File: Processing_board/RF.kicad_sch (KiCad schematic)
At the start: 13 parts, among them J10 CONMHF1-SMD-G-T, U8 BGS13SN8E6327XTSA1

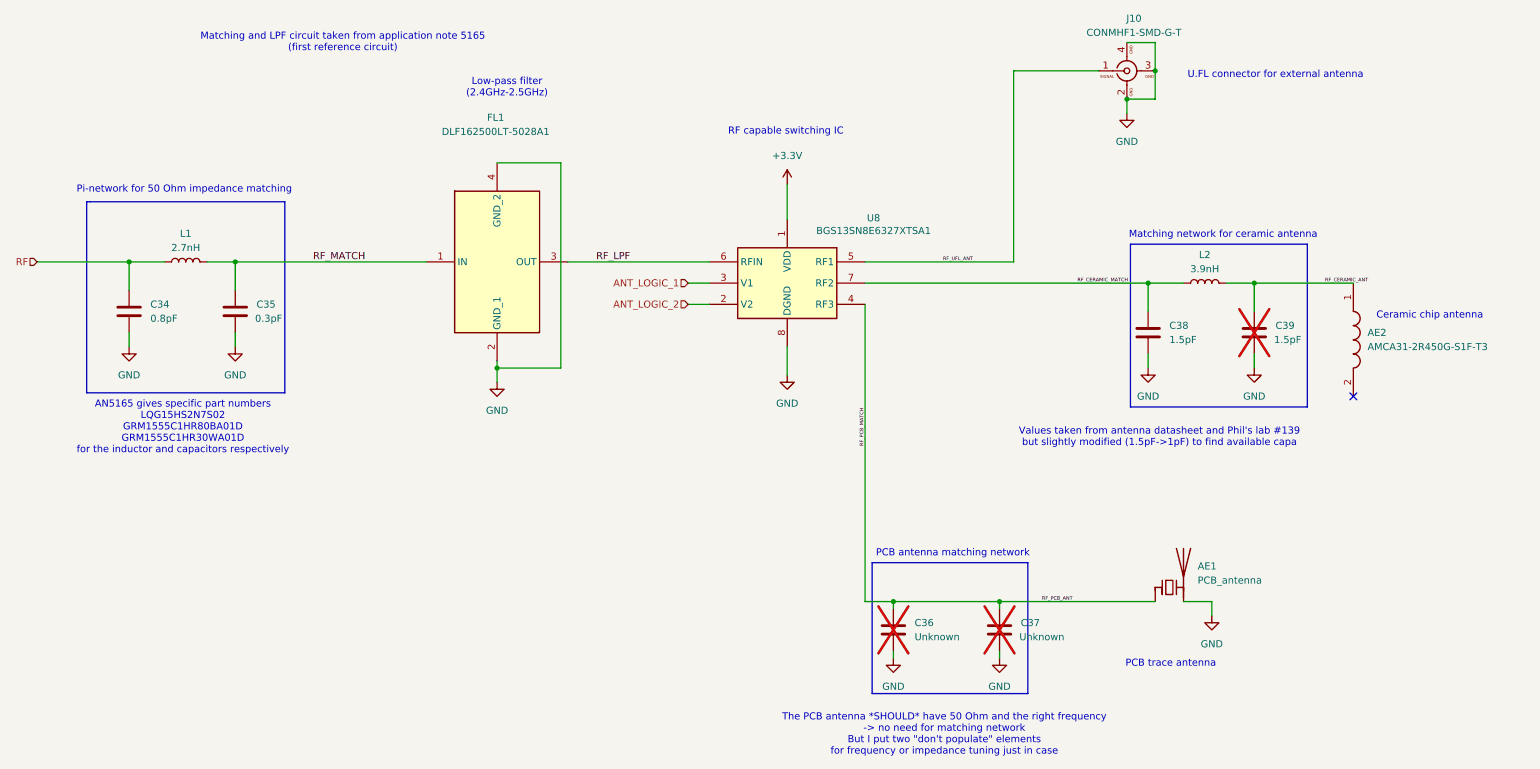
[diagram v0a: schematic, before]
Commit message: RF_circuit schematic updated and board adapted
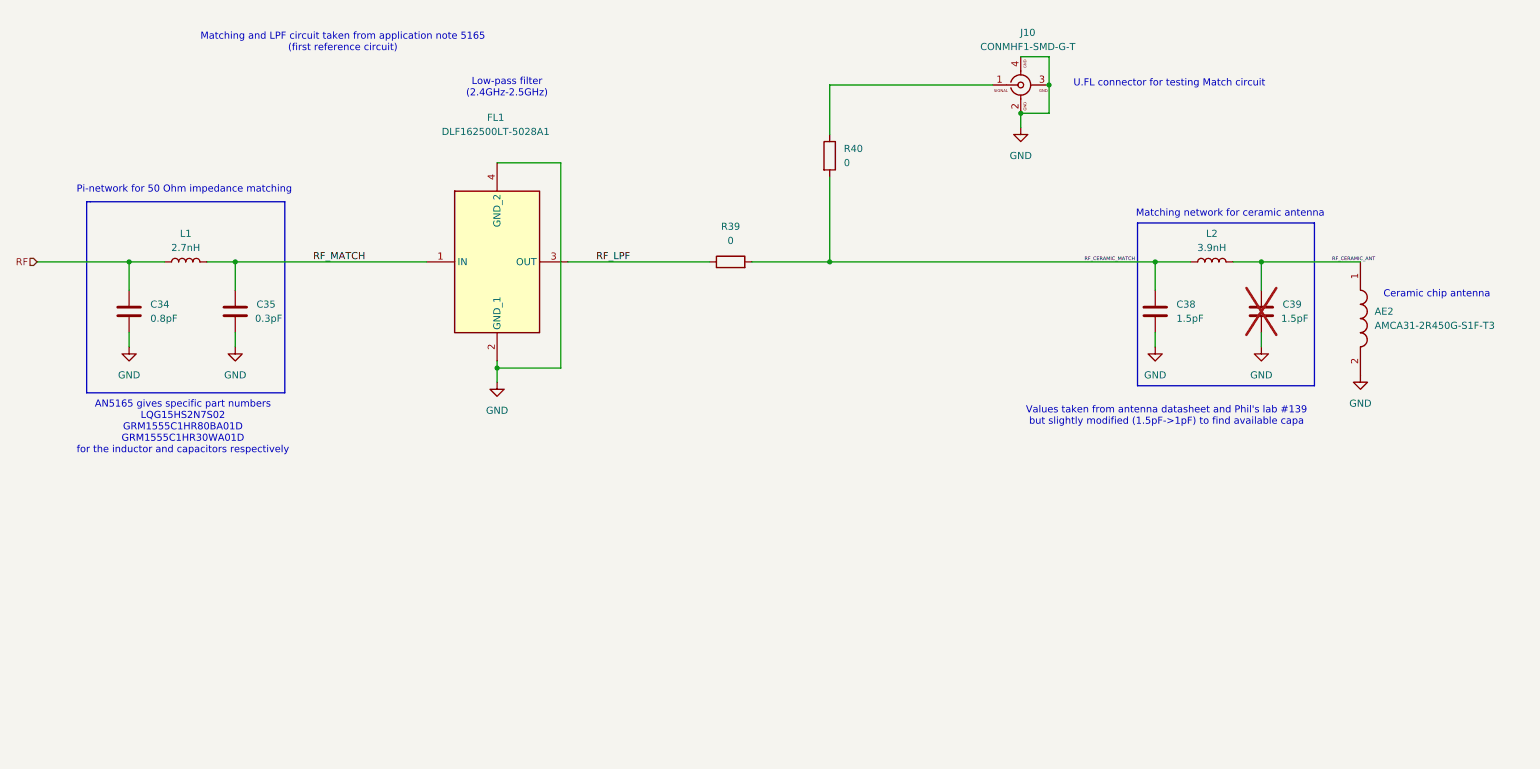
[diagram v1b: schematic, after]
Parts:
- removed AE1: PCB_antenna, RF_Antenna:Texas_SWRA117D_2.4GHz_Left, symbol Device:Antenna_Chip
- removed C36, C37: Unknown, Capacitor_SMD:C_0402_1005Metric, symbol Device:C
- removed U8: BGS13SN8E6327XTSA1, BGS13SN8E6327XTSA1:BGS13SN8E6327XTSA1, symbol BGS13SN8E6327XTSA1:BGS13SN8E6327XTSA1
- added R39, R40: 0, Resistor_SMD:R_0603_1608Metric, symbol Device:R
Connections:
- net GND: now also AE2.2 (NC)
- net RF_CERAMIC_MATCH: now also R39.2, R40.2
- net RF_LPF: now also R39.1
- net RF_UFL_ANT: no longer names the net of J10.1
- net RF_UFL_ANT: now also R40.1
- no-connect marks 1 -> 0
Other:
- note added: "U.FL connector for testing Match circuit"
- note removed: "PCB antenna matching network"
- note removed: "PCB trace antenna"
- note removed: "RF capable switching IC"
- note removed: "The PCB antenna *SHOULD* have 50 Ohm and the right frequency -> no need for matching network But I put two "don't populate" elements for frequency or impedance tuning just in case"
- note removed: "U.FL connector for external antenna"
- moved on the sheet: AE2, C38, C39, J10, L2
